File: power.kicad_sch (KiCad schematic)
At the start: 45 parts, among them U10 INA180A2, U6 TLV62569DBV, U7 XC6206P182MR_C347373, U8 TPS63070RNMR, U9 TPS2121RUXR

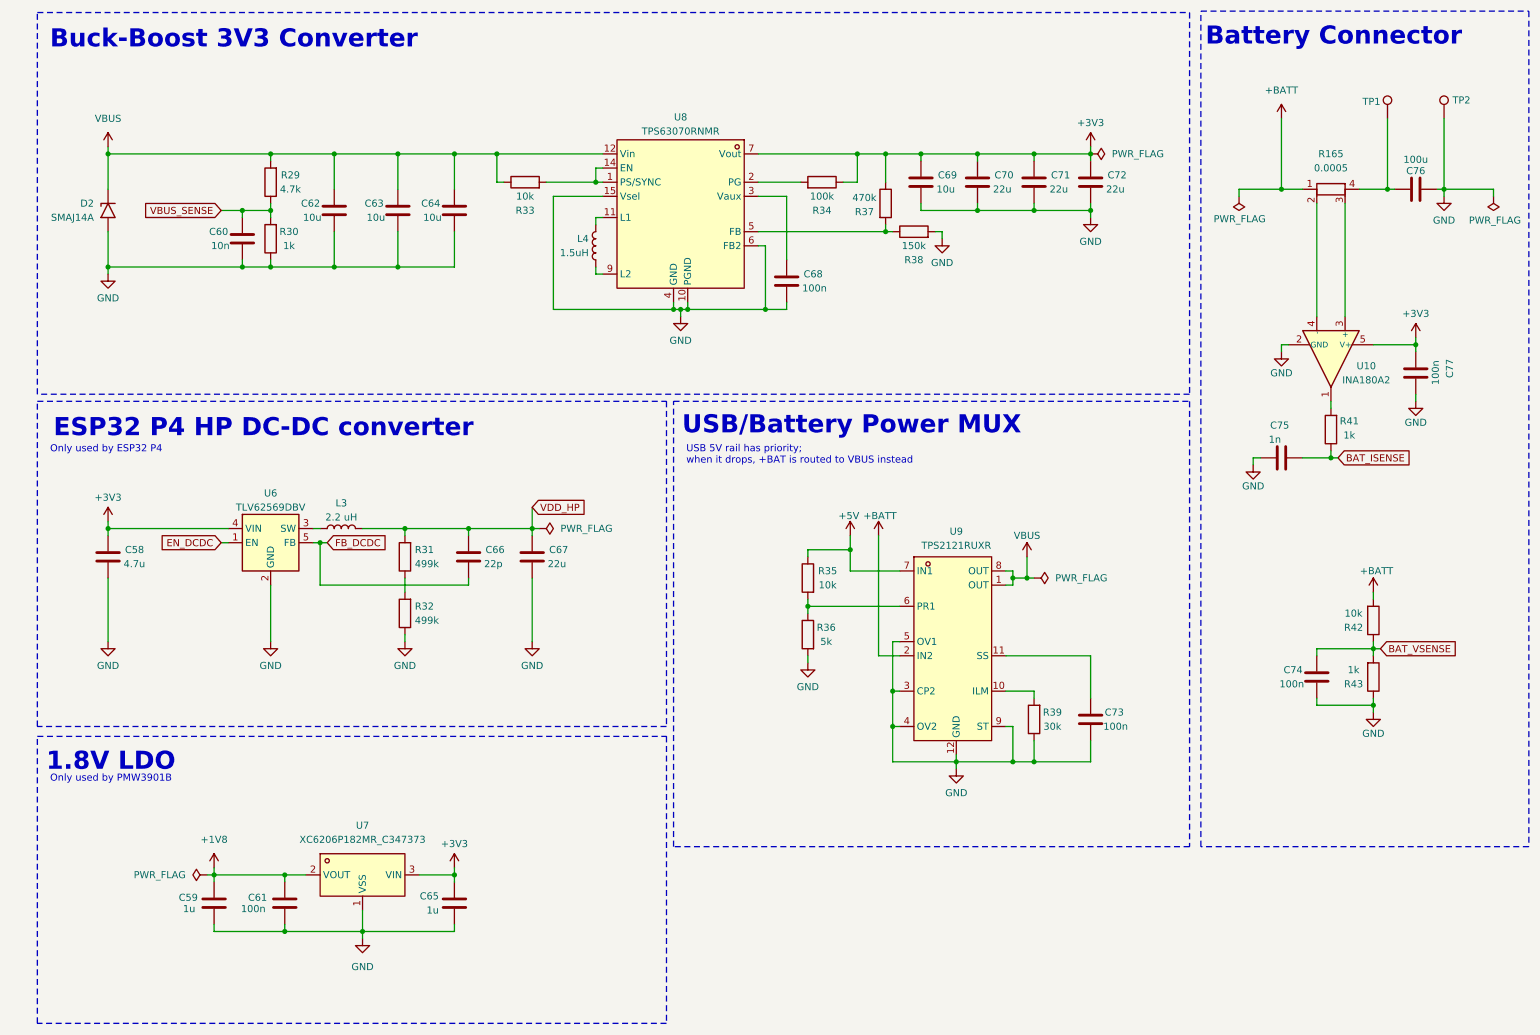
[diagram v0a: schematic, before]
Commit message: Update PCB stackup and design rules
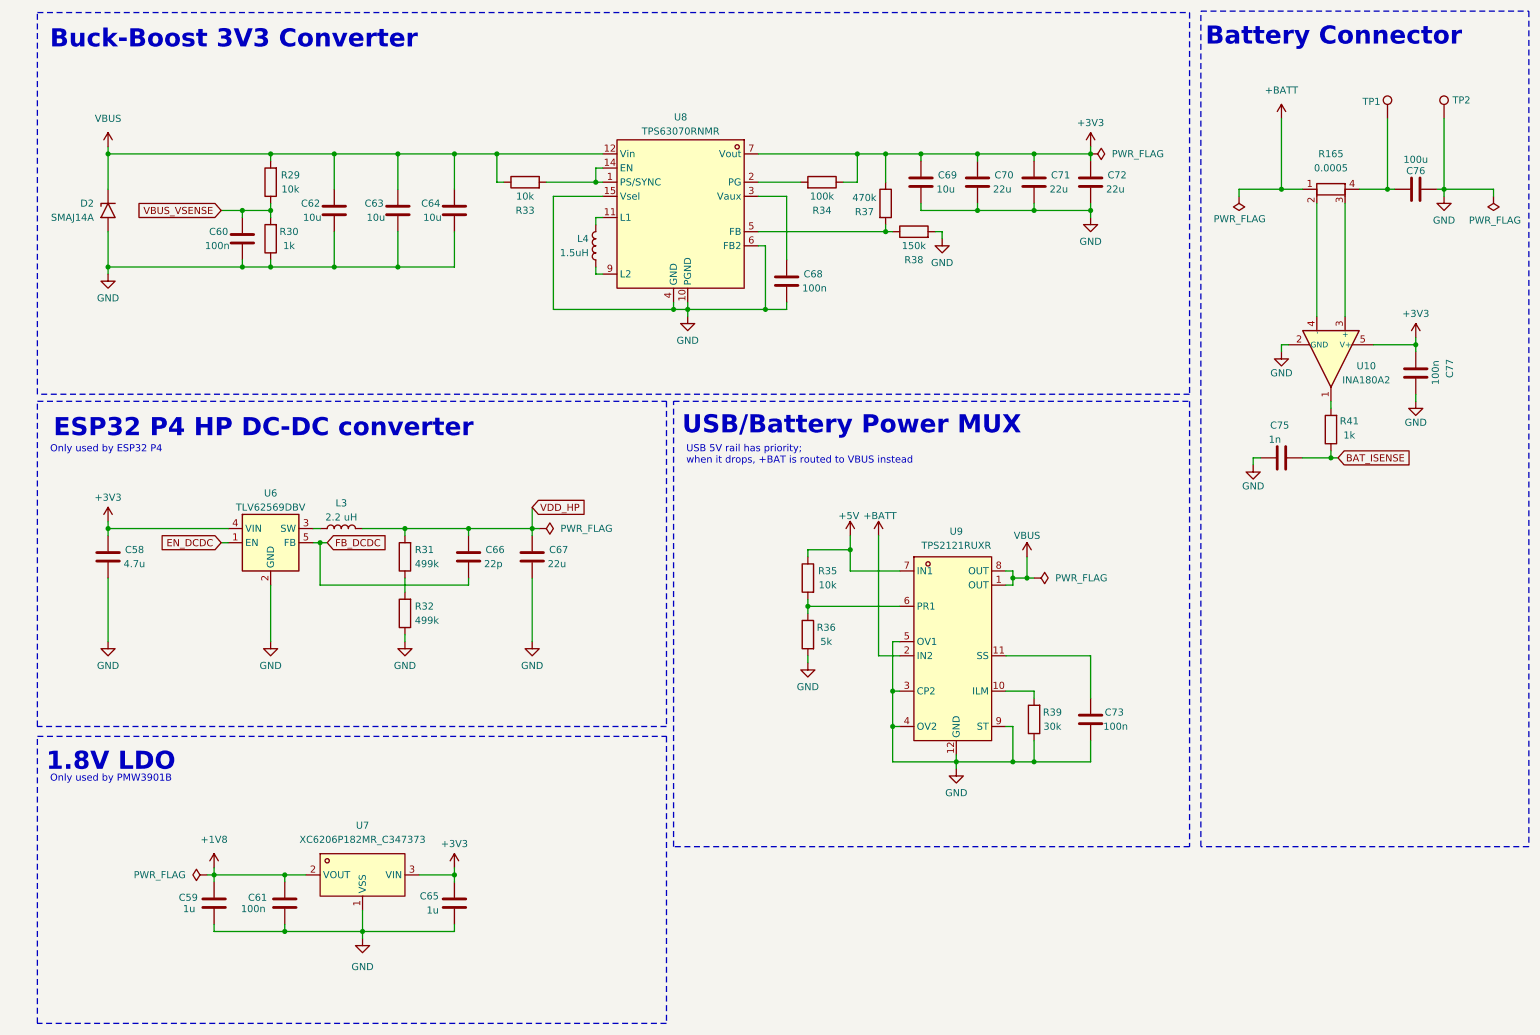
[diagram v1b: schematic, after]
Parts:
- removed C74: 100n, Capacitor_SMD:C_0402_1005Metric, symbol Device:C
- removed R42: 10k, Resistor_SMD:R_0402_1005Metric, symbol Device:R
- removed R43: 1k, Resistor_SMD:R_0402_1005Metric, symbol Device:R
- C60: value 10n -> 100n
- R29: value 4.7k -> 10k
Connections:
- net VBUS_SENSE renamed VBUS_VSENSE

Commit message: Remove a lot of test points
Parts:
- renumbered C75 to C74, C76 to C75, C77 to C76, R35 to R34, R36 to R35, R34 to R36, R165 to R40

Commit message: Remove whole battery current shunt and replace MOSFETs with 3.3x3.3mm alternative
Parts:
- removed C74: 1n, Capacitor_SMD:C_0402_1005Metric, symbol Device:C
- removed C76: 100n, Capacitor_SMD:C_0402_1005Metric, symbol Device:C
- removed R40: 0.0005, Resistor_SMD:R_Shunt_Vishay_WSK2512_6332Metric_T2.66mm, symbol Device:R_Shunt
- removed R41: 1k, Resistor_SMD:R_0402_1005Metric, symbol Device:R
- removed U10: INA180A2, Package_TO_SOT_SMD:SOT-23-5, symbol Amplifier_Current:INA180A2
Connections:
- net +BATT: now also C75.2, TP1.1
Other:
- moved on the sheet: C75, TP1, TP2

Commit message: Improve some connector footprints
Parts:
- removed D2: SMAJ14A, Diode_SMD:D_SMA, symbol Diode:SMAJ14A
- added D2: SMF14A, Diode_SMD:D_SMF, symbol Diode:SMF14A
- TP1, TP2: footprint Connector_Wire:SolderWire-2sqmm_1x01_D2mm_OD3.9mm -> easyeda2kicad:BatteryPad_4x3mm
- renumbered C75 to C74
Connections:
- net GND: now also D2.2 (A2)
- net VBUS: now also D2.1 (A1)
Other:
- moved on the sheet: C74, TP1, TP2

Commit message: Preliminary C5 layout done
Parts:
- C64: footprint Capacitor_SMD:C_0805_2012Metric -> Capacitor_SMD:C_0603_1608Metric
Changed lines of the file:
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@@
 			)
 		)
-		(property "Footprint" "Capacitor_SMD:C_0805_2012Metric"
+		(property "Footprint" "Capacitor_SMD:C_0603_1608Metric"
 			(at 87.9348 53.34 0)
 			(hide yes)

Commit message: Do local layout of power sheet
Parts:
- C69: footprint Capacitor_SMD:C_0805_2012Metric -> Capacitor_SMD:C_0603_1608Metric
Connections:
- net FB_DCDC: now also R31.1, R32.2
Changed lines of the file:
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@@
 	)
 	(junction
+		(at 80.01 116.84)
+		(diameter 0)
+		(color 0 0 0 0)
+	)
+	(junction
 		(at 64.77 109.22)
 		(diameter 0)
@@
 	(wire
 		(pts
-			(xy 80.01 115.57) (xy 80.01 118.11)
-		)
-		(stroke
-			(width 0)
-			(type default)
-		)
-	)
-	(wire
-		(pts
 			(xy 264.16 50.8) (xy 264.16 49.53)
 		)
@@
 	(wire
 		(pts
+			(xy 80.01 116.84) (xy 80.01 118.11)
+		)
+		(stroke
+			(width 0)
+			(type default)
+		)
+	)
+	(wire
+		(pts
 			(xy 161.29 44.45) (xy 161.29 39.37)
 		)
@@
 	(wire
 		(pts
-			(xy 64.77 116.84) (xy 91.44 116.84)
+			(xy 64.77 116.84) (xy 80.01 116.84)
 		)
 		(stroke
@@
 	(wire
 		(pts
+			(xy 80.01 115.57) (xy 80.01 116.84)
+		)
+		(stroke
+			(width 0)
+			(type default)
+		)
+	)
+	(wire
+		(pts
 			(xy 46.99 109.22) (xy 48.26 109.22)
 		)
@@
 	(wire
 		(pts
+			(xy 80.01 116.84) (xy 91.44 116.84)
+		)
+		(stroke
+			(width 0)
+			(type default)
+		)
+	)
+	(wire
+		(pts
 			(xy 88.9 168.91) (xy 88.9 170.18)
 		)
@@
 			)
 		)
-		(property "Footprint" "Capacitor_SMD:C_0805_2012Metric"
+		(property "Footprint" "Capacitor_SMD:C_0603_1608Metric"
 			(at 173.6852 48.26 0)
 			(hide yes)

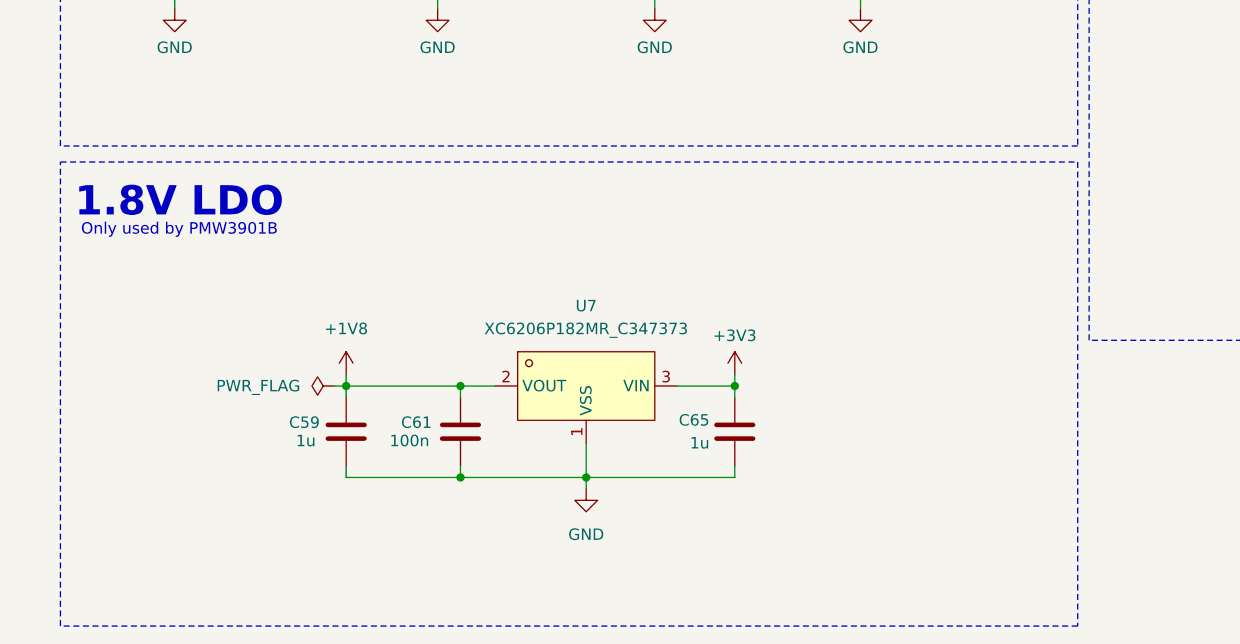
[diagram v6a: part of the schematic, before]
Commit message: Get rid of 1.8V LDO and use P4 VDDO4 instead
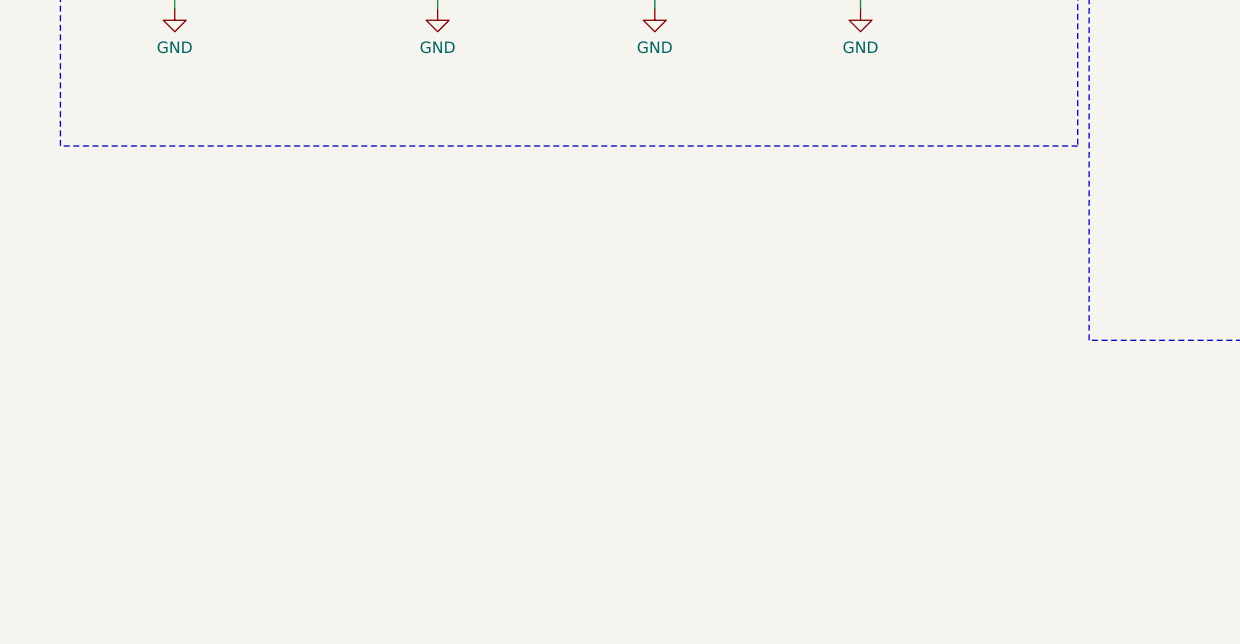
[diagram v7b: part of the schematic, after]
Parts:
- removed C59, C65: 1u, Capacitor_SMD:C_0402_1005Metric, symbol Device:C
- removed C61: 100n, Capacitor_SMD:C_0402_1005Metric, symbol Device:C
- removed U7: XC6206P182MR_C347373, easyeda2kicad:SOT-23-3_L3.0-W1.7-P0.95-LS2.9-BR, symbol easyeda2kicad:XC6206P182MR_C347373
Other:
- note removed: "1.8V LDO"
- note removed: "Only used by PMW3901B"

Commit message: Route buck boost and P4 HP converter
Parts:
- C64: footprint Capacitor_SMD:C_0603_1608Metric -> Capacitor_SMD:C_0805_2012Metric
- C70, C71, C72: footprint Capacitor_SMD:C_0805_2012Metric -> Capacitor_SMD:C_0603_1608Metric
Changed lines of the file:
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@@
 			)
 		)
-		(property "Footprint" "Capacitor_SMD:C_0805_2012Metric"
+		(property "Footprint" "Capacitor_SMD:C_0603_1608Metric"
 			(at 204.1652 48.26 0)
 			(hide yes)
@@
 			)
 		)
-		(property "Footprint" "Capacitor_SMD:C_0805_2012Metric"
+		(property "Footprint" "Capacitor_SMD:C_0603_1608Metric"
 			(at 183.8452 48.26 0)
 			(hide yes)
@@
 			)
 		)
-		(property "Footprint" "Capacitor_SMD:C_0603_1608Metric"
+		(property "Footprint" "Capacitor_SMD:C_0805_2012Metric"
 			(at 87.9348 53.34 0)
 			(hide yes)
@@
 			)
 		)
-		(property "Footprint" "Capacitor_SMD:C_0805_2012Metric"
+		(property "Footprint" "Capacitor_SMD:C_0603_1608Metric"
 			(at 194.0052 48.26 0)
 			(hide yes)
